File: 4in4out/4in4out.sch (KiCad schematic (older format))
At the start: 87 parts, among them IC1 ATTINY2313-P, K10 G5T-1-12VDC, K20 G5T-1-12VDC, K30 G5T-1-12VDC, K40 G5T-1-12VDC, P10 CONN_2, P100 CONN_2, P101 CONN_2, P102 CONN_2, P103 CONN_2, P110 CONN_2, P111 CONN_2, P120 CONN_6, P121 CONN_6, P130 CONN_3X2, P20 CONN_2, P30 CONN_2, P40 CONN_2, P50 CONN_2, P60 CONN_2, P70 CONN_2, P80 CONN_2, Q10 NPN, Q20 NPN, Q30 NPN, Q40 NPN, U50 OPTO-TRANSISTOR, U60 OPTO-TRANSISTOR, U70 OPTO-TRANSISTOR, U80 OPTO-TRANSISTOR

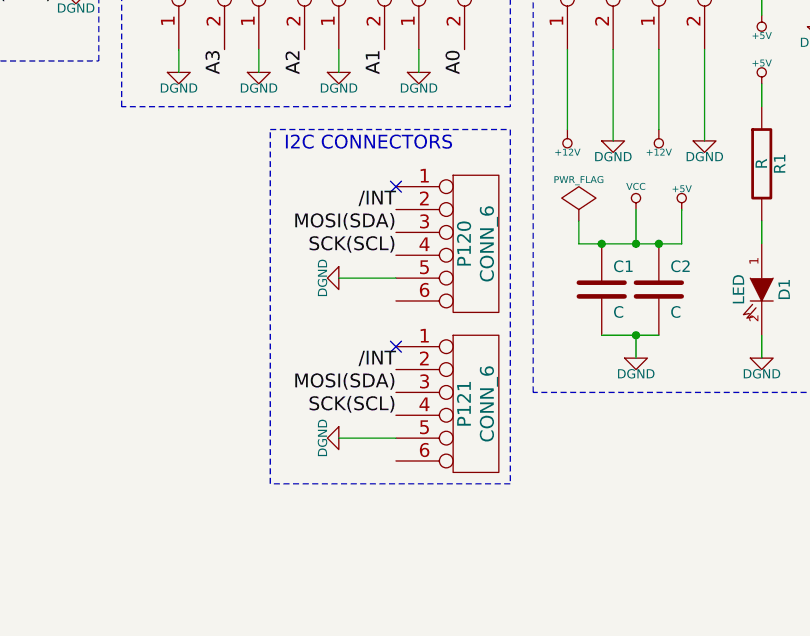
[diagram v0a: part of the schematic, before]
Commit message: PCB 4in4out draft apres refonte
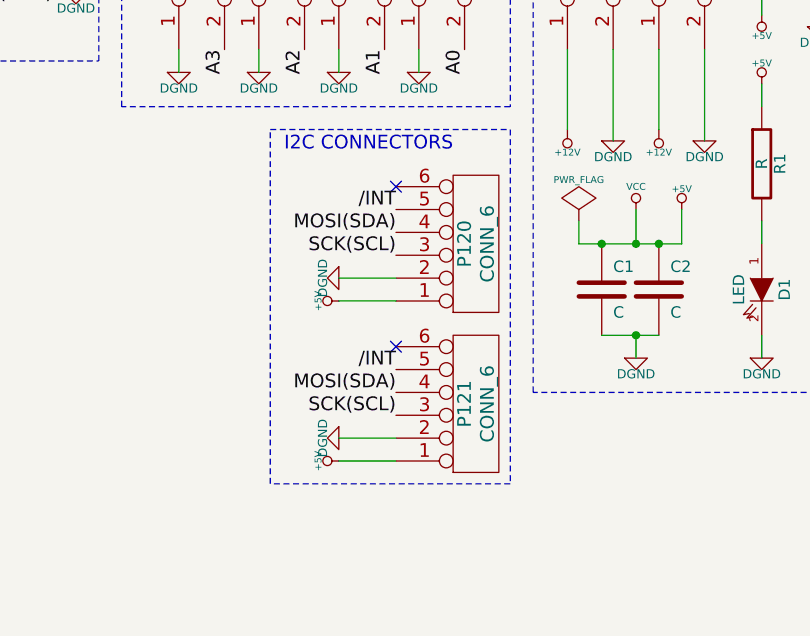
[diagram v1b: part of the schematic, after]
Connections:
- net +5V: now also P120.1, P121.1
- net /INT: now also P120.5, P121.5; no longer P120.2, P121.2
- net DGND: now also P120.2, P121.2; no longer P120.5, P121.5
- net MOSI(SDA): now also P120.4, P121.4; no longer P120.3, P121.3
- net SCK(SCL): now also P120.3, P121.3; no longer P120.4, P121.4
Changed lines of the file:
@@
-EESchema Schematic File Version 2  date mar. 02 oct. 2012 18:53:58 CEST
+EESchema Schematic File Version 2  date mer. 03 oct. 2012 08:24:28 CEST
 LIBS:g5la-1-12vdc
 LIBS:power
@@
 Sheet 1 1
 Title "4in4out i2c board"
-Date "2 oct 2012"
+Date "3 oct 2012"
 Rev "V0.0"
 Comp "XPLDUINO project"
@@
 F 1 "CONN_6" V 9300 2100 60  0000 C CNN
 	1    9250 2100
-	1    0    0    -1
+	1    0    0    1
 $EndComp
 $Comp
@@
 F 1 "CONN_6" V 9300 2800 60  0000 C CNN
 	1    9250 2800
-	1    0    0    -1
+	1    0    0    1
 $EndComp
 NoConn ~ 8900 1850
@@
 	9950 2500 9950 2600
 Connection ~ 9950 2500
+$Comp
+L +5V #PWR047
+U 1 1 506BDD19
+P 8650 2350
+F 0 "#PWR047" H 8650 2440 20  0001 C CNN
+F 1 "+5V" H 8650 2440 30  0000 C CNN
+	1    8650 2350
+	0    -1   -1   0
+$EndComp
+$Comp
+L +5V #PWR048
+U 1 1 506BDD28
+P 8650 3050
+F 0 "#PWR048" H 8650 3140 20  0001 C CNN
+F 1 "+5V" H 8650 3140 30  0000 C CNN
+	1    8650 3050
+	0    -1   -1   0
+$EndComp
+Wire Wire Line
+	8650 3050 8900 3050
+Wire Wire Line
+	8650 2350 8900 2350
 $EndSCHEMATC

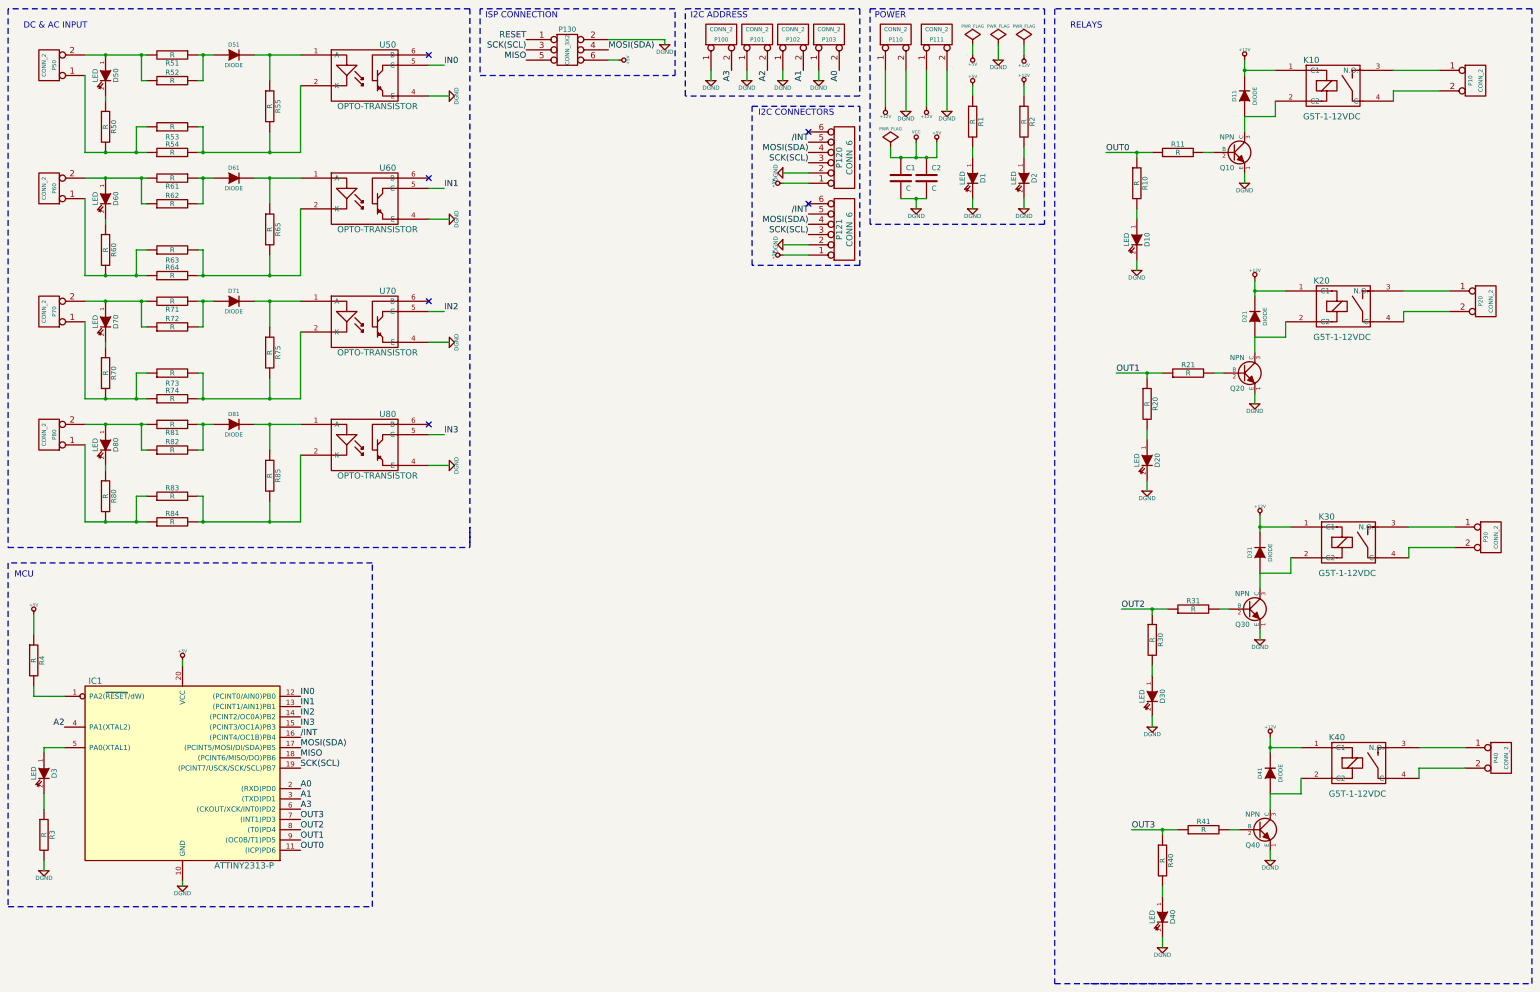
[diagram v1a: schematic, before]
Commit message: Deplacement Resistance led de sortir, mise en place label, am?lioration du plan de masse
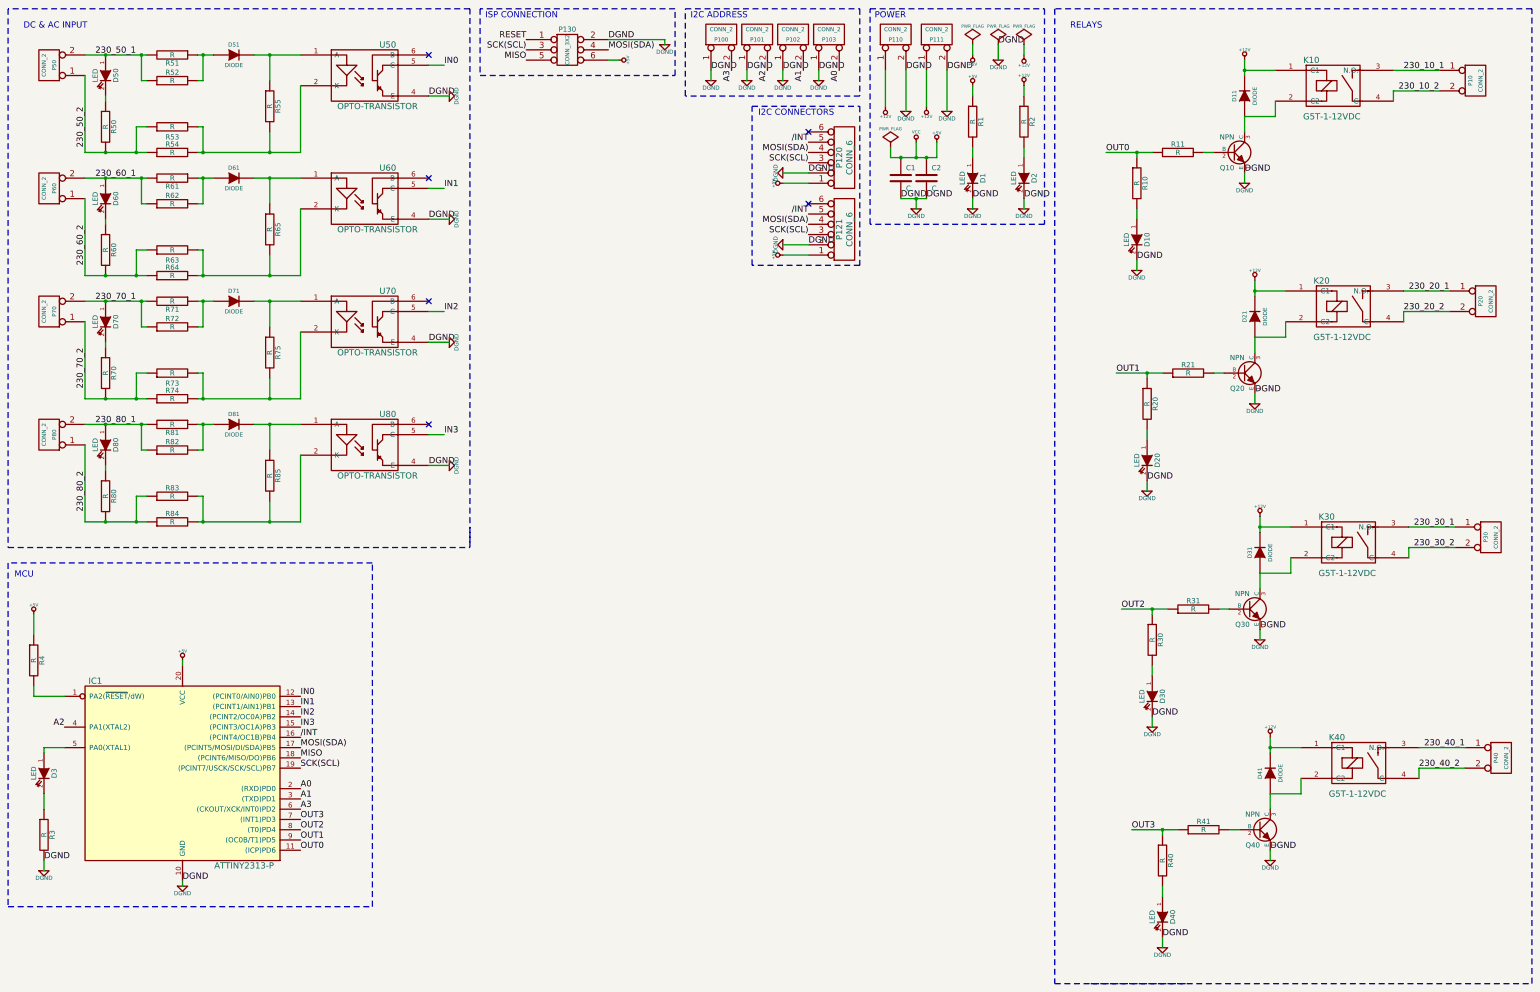
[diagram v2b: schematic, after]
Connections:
- net 230_10_1: now reaches K10.3 (N.O.), P10.1 (P1)
- net 230_10_2: now reaches K10.4 (C), P10.2 (PM)
- net 230_20_1: now reaches K20.3 (N.O.), P20.1 (P1)
- net 230_20_2: now reaches K20.4 (C), P20.2 (PM)
- net 230_30_1: now reaches K30.3 (N.O.), P30.1 (P1)
- net 230_30_2: now reaches K30.4 (C), P30.2 (PM)
- net 230_40_1: now reaches K40.3 (N.O.), P40.1 (P1)
- net 230_40_2: now reaches K40.4 (C), P40.2 (PM)
- net 230_50_1: now reaches D50.1 (A), P50.2 (PM), R51.2, R52.1
- net 230_50_2: now reaches P50.1 (P1), R50.2, R53.1, R54.1
- net 230_60_1: now reaches D60.1 (A), P60.2 (PM), R61.2, R62.1
- net 230_60_2: now reaches P60.1 (P1), R60.2, R63.1, R64.1
- net 230_70_1: now reaches D70.1 (A), P70.2 (PM), R71.2, R72.1
- net 230_70_2: now reaches P70.1 (P1), R70.2, R73.1, R74.1
- net 230_80_1: now reaches D80.1 (A), P80.2 (PM), R81.2, R82.1
- net 230_80_2: now reaches P80.1 (P1), R80.2, R83.1, R84.1
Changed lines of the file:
@@
-EESchema Schematic File Version 2  date mer. 03 oct. 2012 08:24:28 CEST
+EESchema Schematic File Version 2  date mer. 03 oct. 2012 15:48:29 CEST
 LIBS:g5la-1-12vdc
 LIBS:power
@@
 Wire Wire Line
 	8650 2350 8900 2350
+Text Label 14700 1250 0    60   ~ 0
+230_10_1
+Text Label 14650 1450 0    60   ~ 0
+230_10_2
+Text Label 14750 3400 0    60   ~ 0
+230_20_1
+Text Label 14700 3600 0    60   ~ 0
+230_20_2
+Text Label 14800 5700 0    60   ~ 0
+230_30_1
+Text Label 14800 5900 0    60   ~ 0
+230_30_2
+Text Label 14900 7850 0    60   ~ 0
+230_40_1
+Text Label 14850 8050 0    60   ~ 0
+230_40_2
+Text Label 5200 1500 0    60   ~ 0
+DGND
+Text Label 5200 2700 0    60   ~ 0
+DGND
+Text Label 5200 3900 0    60   ~ 0
+DGND
+Text Label 5200 5100 0    60   ~ 0
+DGND
+Text Label 2800 9150 0    60   ~ 0
+DGND
+Text Label 1450 8950 0    60   ~ 0
+DGND
+Text Label 12350 9700 0    60   ~ 0
+DGND
+Text Label 13400 8850 0    60   ~ 0
+DGND
+Text Label 12250 7550 0    60   ~ 0
+DGND
+Text Label 13300 6700 0    60   ~ 0
+DGND
+Text Label 12200 5250 0    60   ~ 0
+DGND
+Text Label 13250 4400 0    60   ~ 0
+DGND
+Text Label 12100 3100 0    60   ~ 0
+DGND
+Text Label 13150 2250 0    60   ~ 0
+DGND
+Text Label 11000 2500 0    60   ~ 0
+DGND
+Text Label 10500 2500 0    60   ~ 0
+DGND
+Text Label 10050 2500 0    60   ~ 0
+DGND
+Text Label 9800 2500 0    60   ~ 0
+DGND
+Text Label 9850 1250 0    60   ~ 0
+DGND
+Text Label 10750 1000 0    60   ~ 0
+DGND
+Text Label 10250 1250 0    60   ~ 0
+DGND
+Text Label 9000 1250 0    60   ~ 0
+DGND
+Text Label 8300 1250 0    60   ~ 0
+DGND
+Text Label 8650 1250 0    60   ~ 0
+DGND
+Text Label 7950 1250 0    60   ~ 0
+DGND
+Text Label 6950 950  0    60   ~ 0
+DGND
+Text Label 8900 2250 0    60   ~ 0
+DGND
+Text Label 8900 2950 0    60   ~ 0
+DGND
+Text Label 1950 1100 0    60   ~ 0
+230_50_1
+Text Label 1950 2300 0    60   ~ 0
+230_60_1
+Text Label 1950 3500 0    60   ~ 0
+230_70_1
+Text Label 1950 4700 0    60   ~ 0
+230_80_1
+Text Label 1850 2000 1    60   ~ 0
+230_50_2
+Text Label 1850 3150 1    60   ~ 0
+230_60_2
+Text Label 1850 4350 1    60   ~ 0
+230_70_2
+Text Label 1850 5550 1    60   ~ 0
+230_80_2
 $EndSCHEMATC
